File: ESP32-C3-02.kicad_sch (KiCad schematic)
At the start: 0 parts

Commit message: finished USB/UART bridge and ESP32 schematic
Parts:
- added C10, C8: 0.1u, symbol Device:C
- added C11: 1u, symbol Device:C
- added C7: 10u, symbol Device:C_Polarized
- added C9: 4.7u, symbol Device:C_Polarized
- added J3: GSD090012SEU, GSD090012SEU:AMPHENOL_GSD090012SEU, symbol GSD090012SEU:GSD090012SEU
- added LED5: LTST-C170GKT, LEDC2012X120N, symbol LTST-C170GKT:LTST-C170GKT
- added LED6: LTST-C170KRKT, LEDC2012X120N, symbol LTST-C170KRKT:LTST-C170KRKT
- added R11: 1k, symbol Device:R
- added R12: 22.1k, symbol Device:R
- added R13: 47.5k, symbol Device:R
- added R14, R18: 470, symbol Device:R
- added R15, R20: 50, symbol Device:R
- added U3: ESP32-C3-WROOM-02-H4, ESP32-C3-WROOM-02-H4:MODULE_ESP32-C3-WROOM-02-H4, symbol ESP32-C3-WROOM-02-H4:ESP32-C3-WROOM-02-H4
- added U4: CP2102N-Axx-xQFN20, Package_DFN_QFN:SiliconLabs_QFN-20-1EP_3x3mm_P0.5mm, symbol Interface_USB:CP2102N-Axx-xQFN20
- added U5: USBLC6-2SC6, Package_TO_SOT_SMD:SOT-23-6, symbol Power_Protection:USBLC6-2SC6
- added U6: W25Q32JVSSIQ, W25Q32JVSSIQ:SOIC127P790X216-8N, symbol W25Q32JVSSIQ:W25Q32JVSSIQ
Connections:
- new net: R20.2, U3.5 (IO6)
- new net: LED5.1 (K), R14.2
- new net: C11.1, R12.2, R13.1, U4.8 (VBUS)
- new net: R14.1, U4.20 (~{TXT}/GPIO.2)
- new net: R15.1, U3.6 (IO7)
- new net: R18.1, U4.19 (~{RXT}/GPIO.3)
- new net: LED6.1 (K), R18.2
- new net: J3.G1 (SHIELD_GND), J3.G2 (SHIELD_GND), J3.G3 (SHIELD_GND), J3.G4 (SHIELD_GND)
- new net: R11.2, U4.9 (~{RST})
- new net +3V3: C10.1, C7.1, C8.1, C9.1, LED5.2 (A), LED6.2 (A), R11.1, U3.1 (3V3), U4.6 (VDD), U4.7 (VREGIN)
- new net BOOT: U3.8 (IO9)
- new net CD_SD: U3.18 (IO0)
- new net CS: U3.10 (IO10)
- new net CTS~: U4.15 (~{CTS})
- new net EN: U3.2 (EN)
- new net GND: C10.2, C11.2, C7.2, C8.2, C9.2, R13.2, U3.19 (GND), U3.20 (GND), U3.21 (GND), U3.22 (GND), U3.23 (GND), U3.24 (GND), U3.25 (GND), U3.26 (GND), U3.27 (GND), U3.28 (GND), U3.29 (GND), U3.30 (GND), U3.31 (GND), U3.32 (GND), U3.33 (GND), U3.34 (GND), U3.35 (GND), U3.36 (GND), U3.37 (GND), U3.38 (GND), U3.39 (GND), U3.9 (GND), U4.12 (GND), U4.21 (GND), U4.3 (GND), U5.2 (GND)
- new net GPIO18: U3.13 (IO18)
- new net GPIO19: U3.14 (IO19)
- new net GPIO8: U3.7 (IO8)
- new net MIC_OUT: U3.4 (IO5)
- new net MISO_DO: U3.16 (IO2)
- new net MOSI_DI: R15.2
- new net PHOTO_C: U3.17 (IO1)
- new net RTS~: U4.16 (~{RTS})
- new net RX_TX: U3.12 (TXD), U4.17 (RXD)
- new net SCL: U3.15 (IO3)
- new net SCLK: R20.1
- new net SDA: U3.3 (IO4)
- new net TX_RX: U3.11 (RXD), U4.18 (TXD)
- new net USB_D+: U4.4 (D+), U5.3 (I/O2)
- new net USB_D-: U4.5 (D-), U5.1 (I/O1)
- new net USB_DN: U5.6 (I/O1)
- new net USB_DP: U5.4 (I/O2)
- new net VBUS: R12.1, U5.5 (VBUS)
- no-connect marks 0 -> 5
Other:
- note added: "CLEAR TO SEND (input)"
- note added: "ESP32"
- note added: "READY TO SEND (output)"
- note added: "USB to UART Bridge"

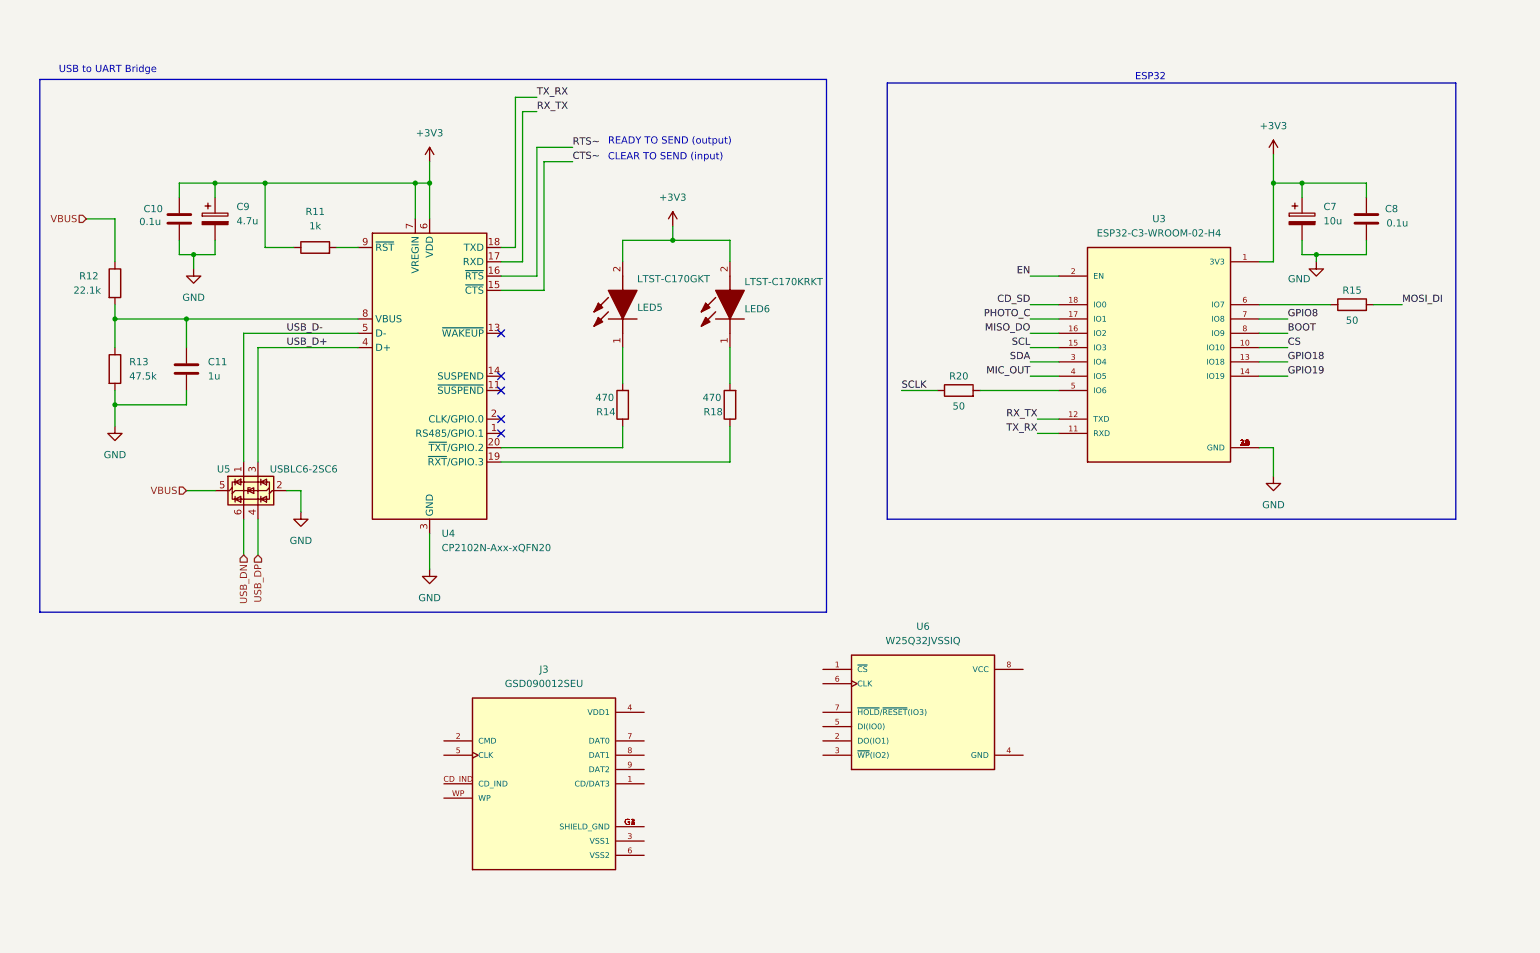
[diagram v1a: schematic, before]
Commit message: finished SD card and flash memory schematic
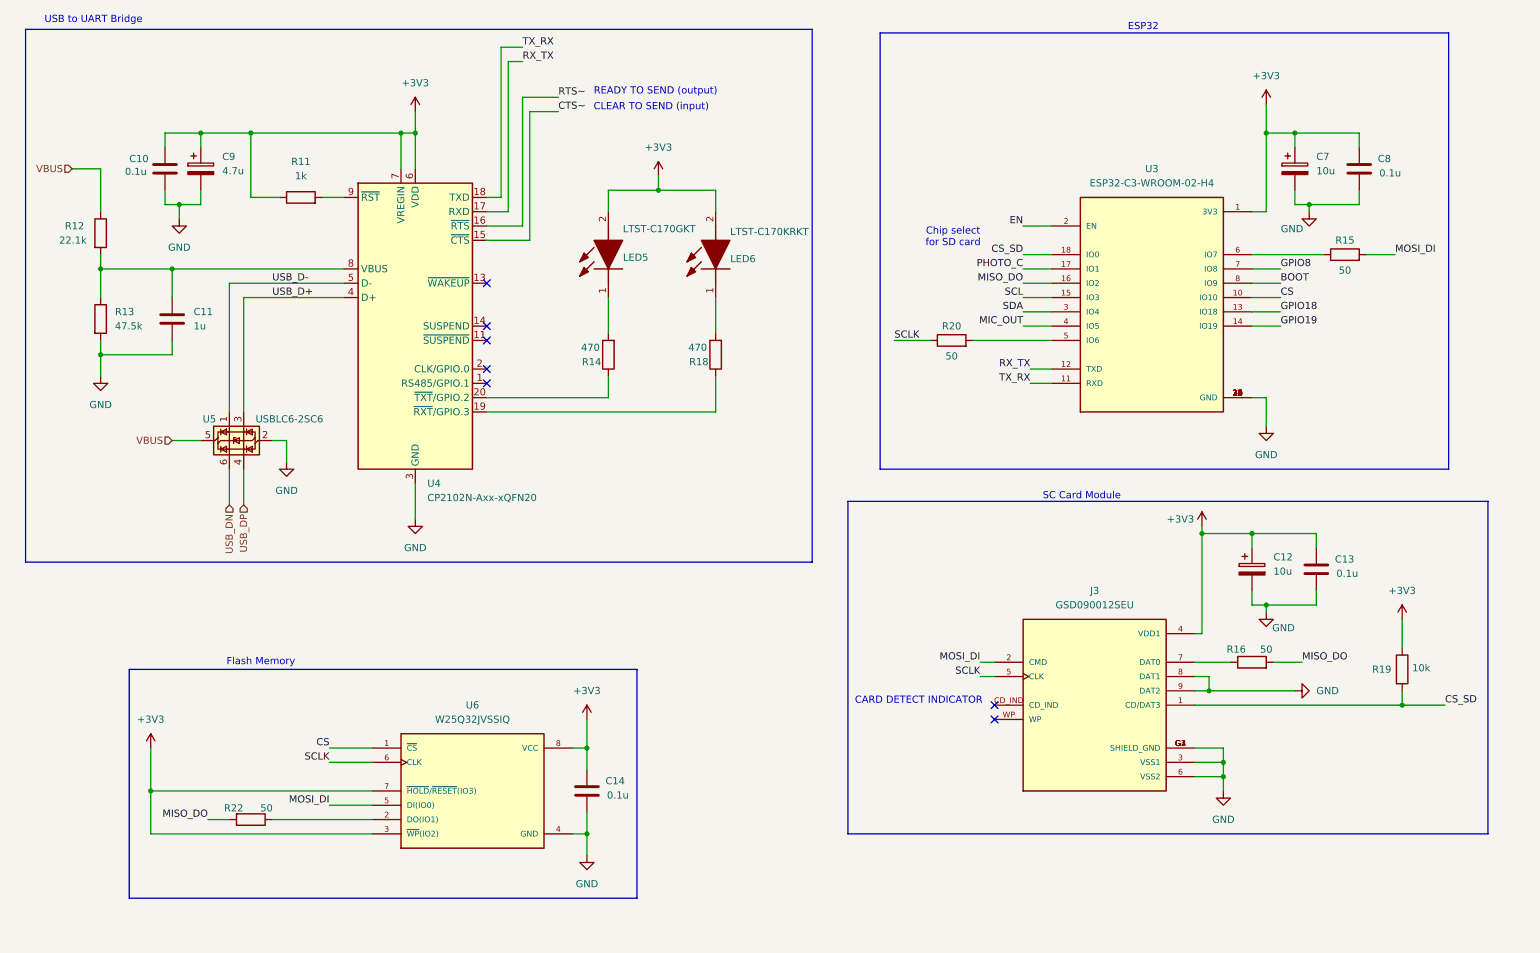
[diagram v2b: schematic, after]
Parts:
- added C12: 10u, symbol Device:C_Polarized
- added C13, C14: 0.1u, symbol Device:C
- added R16, R22: 50, symbol Device:R
- added R19: 10k, symbol Device:R
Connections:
- net CD_SD is gone; now on net CS_SD: U3.18 (IO0)
- net +3V3: now also J3.4 (VDD1), U6.3 (~{WP}(IO2)), U6.7 (~{HOLD}/~{RESET}(IO3)), U6.8 (VCC), C12.1, C13.1, C14.1, R19.1
- net CS: now also U6.1 (~{CS})
- net GND: now also J3.3 (VSS1), J3.6 (VSS2), J3.8 (DAT1), J3.9 (DAT2), J3.G1 (SHIELD_GND), J3.G2 (SHIELD_GND), J3.G3 (SHIELD_GND), J3.G4 (SHIELD_GND), U6.4 (GND), C12.2, C13.2, C14.2
- net MISO_DO: now also R16.2, R22.2
- net MOSI_DI: now also J3.2 (CMD), U6.5 (DI(IO0))
- net SCLK: now also J3.5 (CLK), U6.6 (CLK)
- net at U6.2 (DO(IO1)): now also R22.1
- net CS_SD: now reaches J3.1 (CD/DAT3)
- net CS_SD: now also R19.2
- net at J3.7 (DAT0): now also R16.1
- no-connect marks 5 -> 7
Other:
- note added: "CARD DETECT INDICATOR"
- note added: "Chip select for SD card"
- note added: "Flash Memory"
- note added: "SC Card Module"
- moved on the sheet: C10, C11, C7, C8, C9, J3, LED5, LED6, R11, R12, R13, R14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

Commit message: finished schematic for sensors
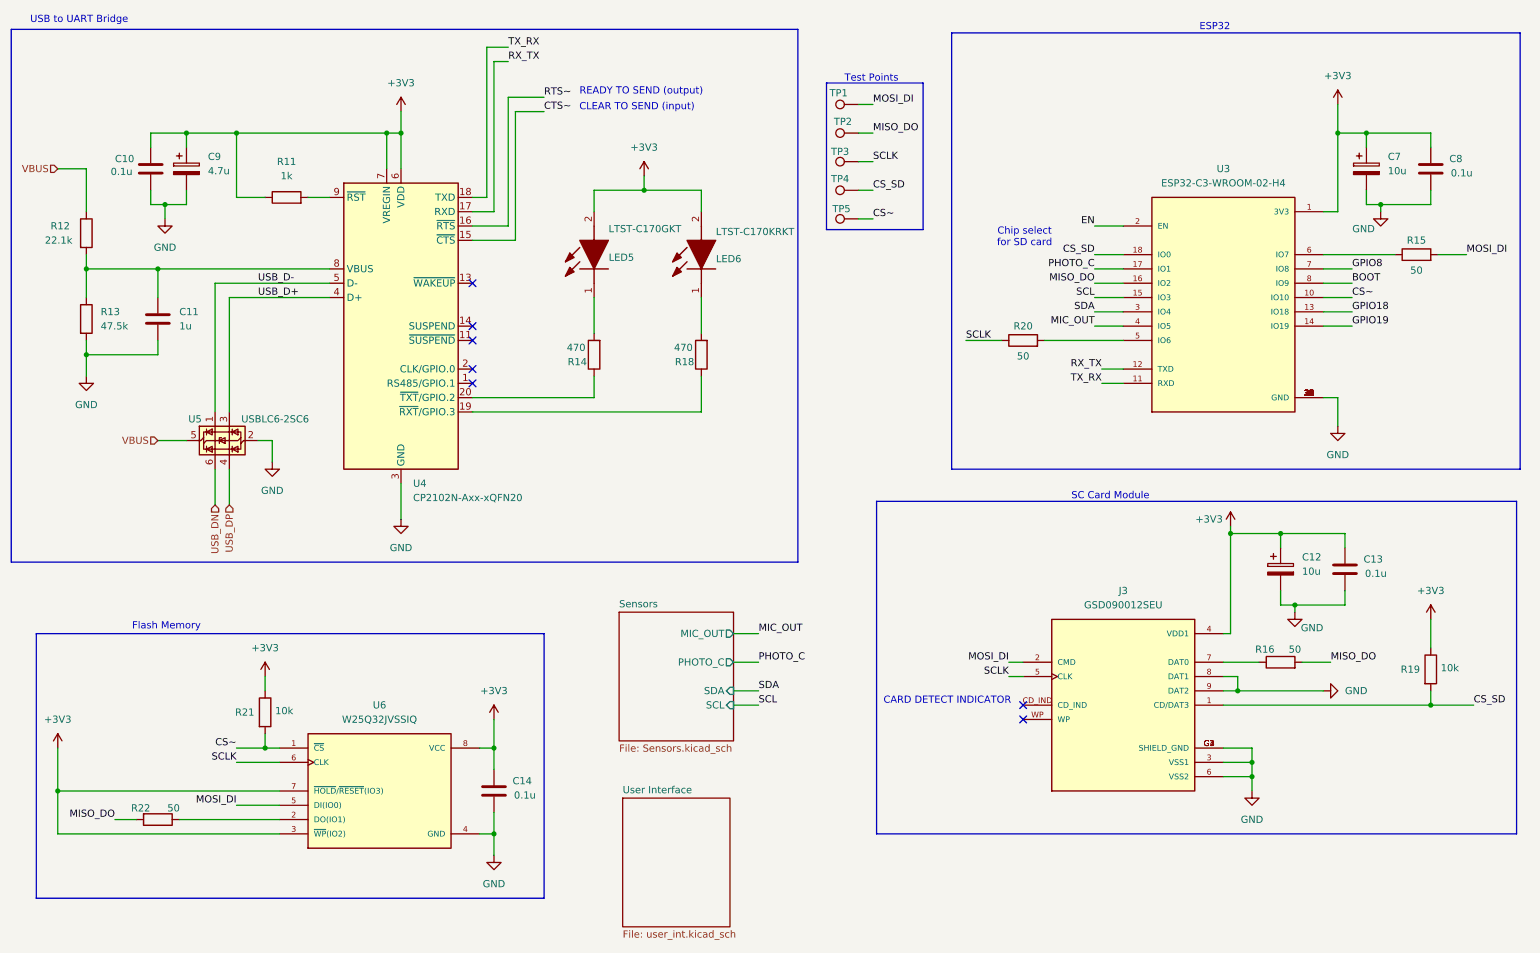
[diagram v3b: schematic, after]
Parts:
- added R21: 10k, symbol Device:R
- added TP1, TP2, TP3, TP4, TP5: TestPoint, symbol Connector:TestPoint
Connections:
- net +3V3: now also R21.1
- net CS_SD: now also TP4.1
- net MISO_DO: now also TP2.1
- net MOSI_DI: now also TP1.1
- net SCLK: now also TP3.1
- net CS renamed CS~
- net CS~: now also R21.2, TP5.1
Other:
- added sheet Sensors (Sensors.kicad_sch)
- added sheet User Interface (user_int.kicad_sch)
- note added: "Test Points"
- title: (none) -> ESP32, USB, SD Card, Flash Memory
- moved on the sheet: C10, C11, C12, C13, C14, C7, C8, C9, J3, LED5, LED6, R11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

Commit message: finished user interface schematic
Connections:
- net CTS~ renamed DTR
- net RTS~ renamed RTS
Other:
- sheet User Interface ports: added BOOT, DTR, EN, GPIO18, GPIO19, GPIO8, RTS, SCL, SDA; removed none
- note removed: "CLEAR TO SEND (input)"

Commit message: setup net classes and started layout
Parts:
- C10, C11, C13, C14, C8: footprint (none) -> Capacitor_SMD:C_0805_2012Metric
- C12, C7, C9: footprint (none) -> ESP32_project_Footprints:T491A
- LED5, LED6: footprint LEDC2012X120N -> ESP32_project_Footprints:LEDC2012X120N
- R11, R12, R13, R14, R15, R16, R18, R19, R20, R21, R22: footprint (none) -> Resistor_SMD:R_0805_2012Metric
- TP1, TP2, TP3, TP4, TP5: footprint (none) -> TestPoint:TestPoint_Pad_D1.0mm
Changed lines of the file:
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@@
 			)
 		)
-		(property "Footprint" ""
+		(property "Footprint" "ESP32_project_Footprints:T491A"
 			(at 256.2352 49.53 0)
 			(hide yes)
@@
 			)
 		)
-		(property "Footprint" ""
+		(property "Footprint" "Resistor_SMD:R_0805_2012Metric"
 			(at 194.31 77.978 90)
 			(hide yes)
@@
 			)
 		)
-		(property "Footprint" "LEDC2012X120N"
+		(property "Footprint" "ESP32_project_Footprints:LEDC2012X120N"
 			(at 211.76 55.88 0)
 			(hide yes)
@@
 			)
 		)
-		(property "Footprint" ""
+		(property "Footprint" "Resistor_SMD:R_0805_2012Metric"
 			(at 264.922 134.62 90)
 			(hide yes)
@@
 			)
 		)
-		(property "Footprint" ""
+		(property "Footprint" "Capacitor_SMD:C_0805_2012Metric"
 			(at 101.2952 160.02 0)
 			(hide yes)
@@
 			)
 		)
-		(property "Footprint" ""
+		(property "Footprint" "Resistor_SMD:R_0805_2012Metric"
 			(at 40.64 159.512 90)
 			(hide yes)
@@
 			)
 		)
-		(property "Footprint" ""
+		(property "Footprint" "Resistor_SMD:R_0805_2012Metric"
 			(at 26.162 57.15 90)
 			(hide yes)
@@
 			)
 		)
-		(property "Footprint" ""
+		(property "Footprint" "ESP32_project_Footprints:T491A"
 			(at 240.9952 120.65 0)
 			(hide yes)
@@
 			)
 		)
-		(property "Footprint" ""
+		(property "Footprint" "Capacitor_SMD:C_0805_2012Metric"
 			(at 40.3352 49.53 0)
 			(hide yes)
@@
 			)
 		)
-		(property "Footprint" ""
+		(property "Footprint" "TestPoint:TestPoint_Pad_D1.0mm"
 			(at 165.1 39.37 0)
 			(hide yes)
@@
 			)
 		)
-		(property "Footprint" ""
+		(property "Footprint" "ESP32_project_Footprints:T491A"
 			(at 46.6852 49.53 0)
 			(hide yes)
@@
 			)
 		)
-		(property "Footprint" ""
+		(property "Footprint" "Resistor_SMD:R_0805_2012Metric"
 			(at 119.888 78.74 90)
 			(hide yes)
@@
 			)
 		)
-		(property "Footprint" ""
+		(property "Footprint" "Capacitor_SMD:C_0805_2012Metric"
 			(at 267.6652 49.53 0)
 			(hide yes)
@@
 			)
 		)
-		(property "Footprint" ""
+		(property "Footprint" "TestPoint:TestPoint_Pad_D1.0mm"
 			(at 165.1 49.53 0)
 			(hide yes)
@@
 			)
 		)
-		(property "Footprint" ""
+		(property "Footprint" "Capacitor_SMD:C_0805_2012Metric"
 			(at 41.6052 76.2 0)
 			(hide yes)
@@
 			)
 		)
-		(property "Footprint" ""
+		(property "Footprint" "Resistor_SMD:R_0805_2012Metric"
 			(at 264.16 62.738 90)
 			(hide yes)
@@
 			)
 		)
-		(property "Footprint" ""
+		(property "Footprint" "Resistor_SMD:R_0805_2012Metric"
 			(at 240.03 135.128 90)
 			(hide yes)
@@
 			)
 		)
-		(property "Footprint" ""
+		(property "Footprint" "Resistor_SMD:R_0805_2012Metric"
 			(at 57.912 142.24 90)
 			(hide yes)
@@
 			)
 		)
-		(property "Footprint" ""
+		(property "Footprint" "Resistor_SMD:R_0805_2012Metric"
 			(at 138.938 78.74 90)
 			(hide yes)
@@
 			)
 		)
-		(property "Footprint" ""
+		(property "Footprint" "Resistor_SMD:R_0805_2012Metric"
 			(at 26.162 72.39 90)
 			(hide yes)
@@
 			)
 		)
-		(property "Footprint" ""
+		(property "Footprint" "TestPoint:TestPoint_Pad_D1.0mm"
 			(at 165.1 29.21 0)
 			(hide yes)
@@
 			)
 		)
-		(property "Footprint" ""
+		(property "Footprint" "TestPoint:TestPoint_Pad_D1.0mm"
 			(at 165.1 34.29 0)
 			(hide yes)
@@
 			)
 		)
-		(property "Footprint" "LEDC2012X120N"
+		(property "Footprint" "ESP32_project_Footprints:LEDC2012X120N"
 			(at 230.81 55.88 0)
 			(hide yes)
@@
 			)
 		)
-		(property "Footprint" ""
+		(property "Footprint" "TestPoint:TestPoint_Pad_D1.0mm"
 			(at 165.1 44.45 0)
 			(hide yes)
@@
 			)
 		)
-		(property "Footprint" ""
+		(property "Footprint" "Resistor_SMD:R_0805_2012Metric"
 			(at 63.5 52.578 90)
 			(hide yes)
@@
 			)
 		)
-		(property "Footprint" ""
+		(property "Footprint" "Capacitor_SMD:C_0805_2012Metric"
 			(at 252.4252 120.65 0)
 			(hide yes)

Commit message: imported all footprints into layout
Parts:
- J3: footprint GSD090012SEU:AMPHENOL_GSD090012SEU -> ESP32_project_Footprints:AMPHENOL_GSD090012SEU; Availability In Stock -> (none); Package None -> (none); Price None -> (none)
- U3: footprint ESP32-C3-WROOM-02-H4:MODULE_ESP32-C3-WROOM-02-H4 -> ESP32_project_Footprints:MODULE_ESP32-C3-WROOM-02-H4; Availability In Stock -> (none); Package Package -> (none); Price None -> (none); Purchase-URL https://pricing.snapeda.com/search/part/ESP32-C3-WROOM-02-H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 -> (none)
- U4: footprint Package_DFN_QFN:SiliconLabs_QFN-20-1EP_3x3mm_P0.5mm -> Package_DFN_QFN:SiliconLabs_QFN-20-1EP_3x3mm_P0.5mm_EP1.8x1.8mm
- U6: footprint W25Q32JVSSIQ:SOIC127P790X216-8N -> ESP32_project_Footprints:SOIC127P790X216-8N; Availability In Stock -> (none); Package SOIC-8 Winbond -> (none); Price None -> (none)
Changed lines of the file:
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@@
 			)
 		)
-		(property "Footprint" "W25Q32JVSSIQ:SOIC127P790X216-8N"
+		(property "Footprint" "ESP32_project_Footprints:SOIC127P790X216-8N"
 			(at 80.01 156.21 0)
 			(hide yes)
@@
 			)
 		)
-		(property "Package" "SOIC-8 Winbond"
-			(at 80.01 156.21 0)
-			(hide yes)
-			(show_name no)
-			(do_not_autoplace no)
-			(effects
-				(font
-					(size 1.27 1.27)
-				)
-				(justify bottom)
-			)
-		)
-		(property "Price" "None"
-			(at 80.01 156.21 0)
-			(hide yes)
-			(show_name no)
-			(do_not_autoplace no)
-			(effects
-				(font
-					(size 1.27 1.27)
-				)
-				(justify bottom)
-			)
-		)
 		(property "SnapEDA_Link" "https://www.snapeda.com/parts/W25Q32JVSSIQ/Winbond+Electronics/view-part/?ref=snap"
 			(at 80.01 156.21 0)
@@
 		)
 		(property "M_PART_NUMBER" "W25QXX"
-			(at 80.01 156.21 0)
-			(hide yes)
-			(show_name no)
-			(do_not_autoplace no)
-			(effects
-				(font
-					(size 1.27 1.27)
-				)
-				(justify bottom)
-			)
-		)
-		(property "Availability" "In Stock"
 			(at 80.01 156.21 0)
 			(hide yes)
@@
 			)
 		)
-		(property "Footprint" "GSD090012SEU:AMPHENOL_GSD090012SEU"
+		(property "Footprint" "ESP32_project_Footprints:AMPHENOL_GSD090012SEU"
 			(at 212.09 140.97 0)
 			(hide yes)
@@
 			)
 		)
-		(property "Package" "None"
-			(at 212.09 140.97 0)
-			(hide yes)
-			(show_name no)
-			(do_not_autoplace no)
-			(effects
-				(font
-					(size 1.27 1.27)
-				)
-				(justify bottom)
-			)
-		)
-		(property "Price" "None"
-			(at 212.09 140.97 0)
-			(hide yes)
-			(show_name no)
-			(do_not_autoplace no)
-			(effects
-				(font
-					(size 1.27 1.27)
-				)
-				(justify bottom)
-			)
-		)
 		(property "Check_prices" "https://www.snapeda.com/parts/GSD090012SEU/Amphenol/view-part/?ref=eda"
 			(at 212.09 140.97 0)
@@
 		)
 		(property "MP" "GSD090012SEU"
-			(at 212.09 140.97 0)
-			(hide yes)
-			(show_name no)
-			(do_not_autoplace no)
-			(effects
-				(font
-					(size 1.27 1.27)
-				)
-				(justify bottom)
-			)
-		)
-		(property "Availability" "In Stock"
 			(at 212.09 140.97 0)
 			(hide yes)
@@
 			)
 		)
-		(property "Footprint" "Package_DFN_QFN:SiliconLabs_QFN-20-1EP_3x3mm_P0.5mm"
+		(property "Footprint" "Package_DFN_QFN:SiliconLabs_QFN-20-1EP_3x3mm_P0.5mm_EP1.8x1.8mm"
 			(at 115.57 100.33 0)
 			(hide yes)
@@
 			)
 		)
-		(property "Footprint" "ESP32-C3-WROOM-02-H4:MODULE_ESP32-C3-WROOM-02-H4"
+		(property "Footprint" "ESP32_project_Footprints:MODULE_ESP32-C3-WROOM-02-H4"
 			(at 229.87 71.12 0)
 			(hide yes)
@@
 			)
 		)
-		(property "Package" "Package"
-			(at 229.87 71.12 0)
-			(hide yes)
-			(show_name no)
-			(do_not_autoplace no)
-			(effects
-				(font
-					(size 1.27 1.27)
-				)
-				(justify bottom)
-			)
-		)
-		(property "Price" "None"
-			(at 229.87 71.12 0)
-			(hide yes)
-			(show_name no)
-			(do_not_autoplace no)
-			(effects
-				(font
-					(size 1.27 1.27)
-				)
-				(justify bottom)
-			)
-		)
 		(property "Check_prices" "https://www.snapeda.com/parts/ESP32-C3-WROOM-02-H4/Espressif+Systems/view-part/?ref=eda"
 			(at 229.87 71.12 0)
@@
 			(at 229.87 71.12 0)
 			(hide yes)
-			(show_name no)
-			(do_not_autoplace no)
-			(effects
-				(font
-					(size 1.27 1.27)
-				)
-				(justify bottom)
-			)
-		)
-		(property "Availability" "In Stock"
-			(at 229.87 71.12 0)
-			(hide yes)
-			(show_name no)
-			(do_not_autoplace no)
-			(effects
-				(font
-					(size 1.27 1.27)
-				)
-				(justify bottom)
-			)
-		)
-		(property "Purchase-URL" "https://pricing.snapeda.com/search/part/ESP32-C3-WROOM-02-H4/?ref=eda"
-			(at 229.87 71.12 0)
-			(hide yes)
